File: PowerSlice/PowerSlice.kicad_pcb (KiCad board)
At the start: 2 copper layers, 9 parts, among them U1 PTH08080WAD, U2 PTH08080WAD, U3 INA214BIDCKR, U4 INA214BIDCKR, U5 INA214BIDCKR, U6 NUCLEO-F303K8

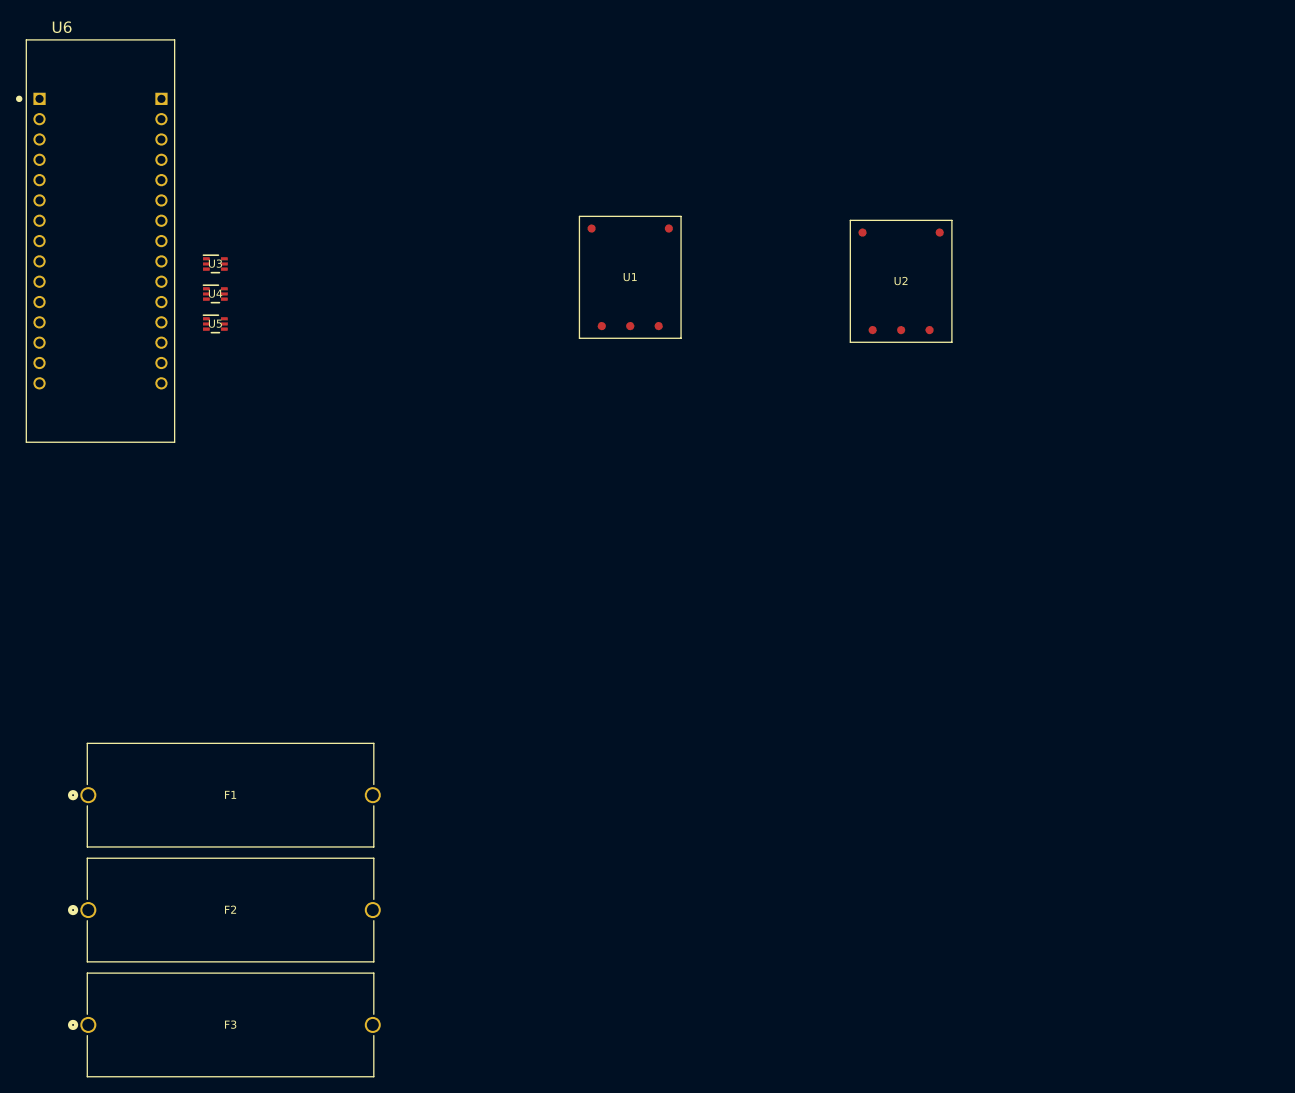
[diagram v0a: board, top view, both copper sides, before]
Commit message: Updated schematic + built PCB
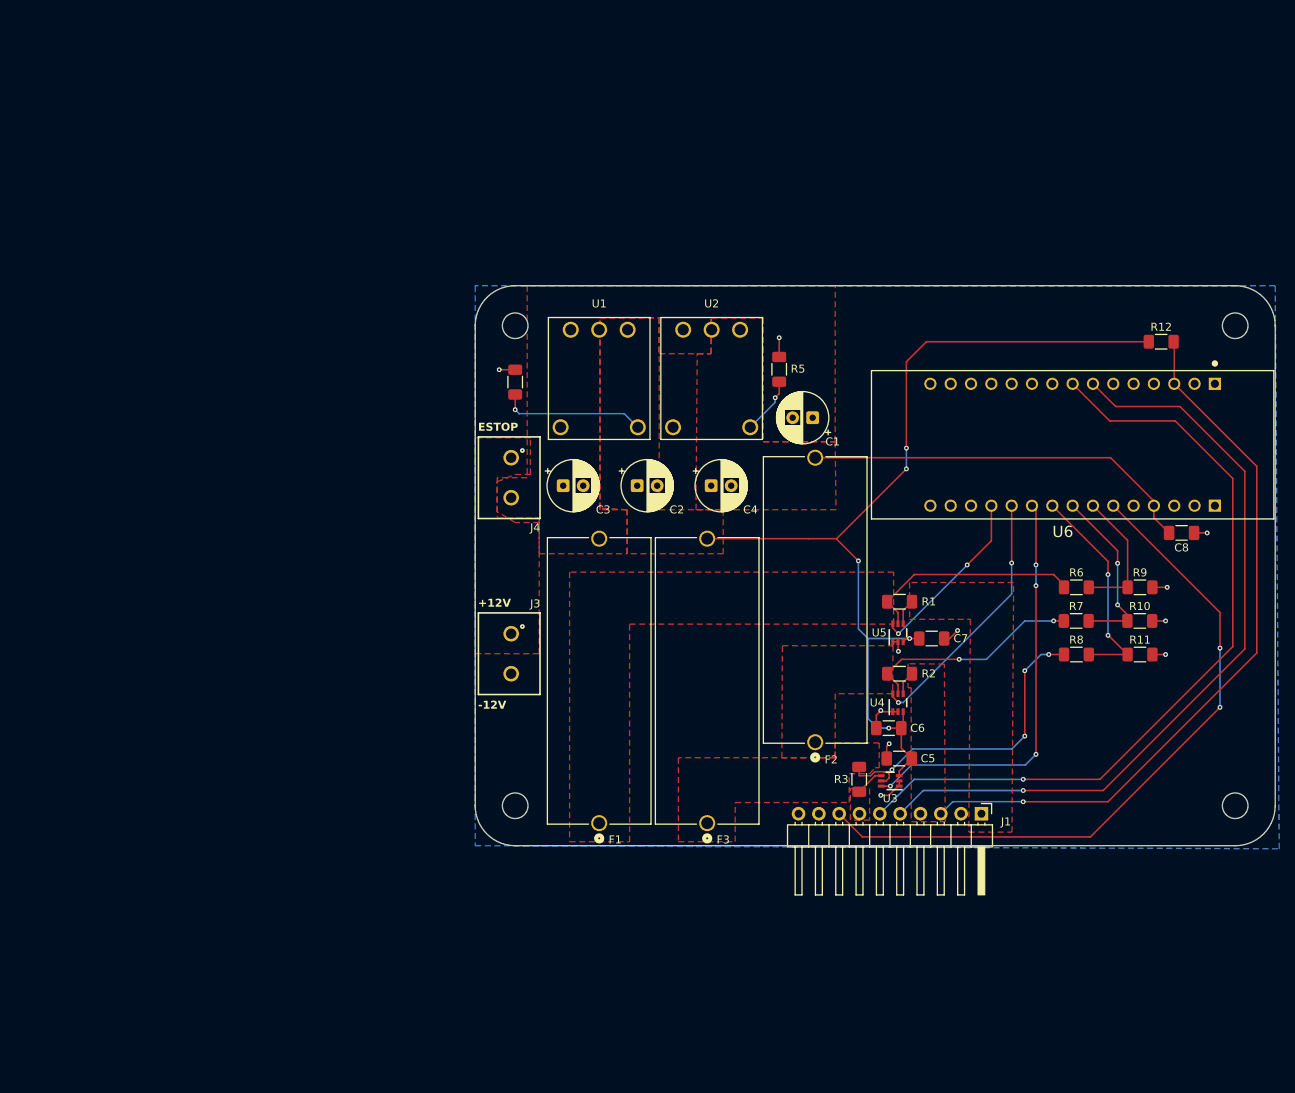
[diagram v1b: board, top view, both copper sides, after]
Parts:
- added C1: 100uF, Capacitor_THT:CP_Radial_D6.3mm_P2.50mm, F.Cu at (116.6, 79.0)
- added C2: 100uF, Capacitor_THT:CP_Radial_D6.3mm_P2.50mm, F.Cu at (94.7, 87.5)
- added C3: 100uF, Capacitor_THT:CP_Radial_D6.3mm_P2.50mm, F.Cu at (85.4, 87.5)
- added C4: 100uF, Capacitor_THT:CP_Radial_D6.3mm_P2.50mm, F.Cu at (103.9, 87.5)
- added C5: 0.1uF, Capacitor_SMD:C_1206_3216Metric_Pad1.33x1.80mm_HandSolder, F.Cu at (127.4, 121.6)
- added C6: 0.1uF, Capacitor_SMD:C_1206_3216Metric_Pad1.33x1.80mm_HandSolder, F.Cu at (126.1, 117.8)
- added C7: 0.1uF, Capacitor_SMD:C_1206_3216Metric_Pad1.33x1.80mm_HandSolder, F.Cu at (131.5, 106.6)
- added C8: 0.1uF, Capacitor_SMD:C_1206_3216Metric_Pad1.33x1.80mm_HandSolder, F.Cu at (162.7, 93.4)
- added J1: Conn_01x10_Pin, Connector_PinHeader_2.54mm:PinHeader_1x10_P2.54mm_Horizontal, F.Cu at (137.7, 128.5)
- added J3: DC_In_Screw, 691137710002:691137710002, F.Cu at (78.9, 108.5)
- added J4: ESTOP, 691137710002:691137710002, F.Cu at (78.9, 86.5)
- added R1: 0.01, Resistor_SMD:R_1206_3216Metric_Pad1.30x1.75mm_HandSolder, F.Cu at (127.5, 102.0)
- added R10: 100k, Resistor_SMD:R_1206_3216Metric_Pad1.30x1.75mm_HandSolder, F.Cu at (157.5, 104.4)
- added R11: 100k, Resistor_SMD:R_1206_3216Metric_Pad1.30x1.75mm_HandSolder, F.Cu at (157.5, 108.6)
- added R12: 100k, Resistor_SMD:R_1206_3216Metric_Pad1.30x1.75mm_HandSolder, F.Cu at (160.2, 69.5)
- added R2: 0.01, Resistor_SMD:R_1206_3216Metric_Pad1.30x1.75mm_HandSolder, F.Cu at (127.5, 111.0)
- added R3: 0.01, Resistor_SMD:R_1206_3216Metric_Pad1.30x1.75mm_HandSolder, F.Cu at (122.4, 124.2)
- added R4: 1.87k, Resistor_SMD:R_1206_3216Metric_Pad1.30x1.75mm_HandSolder, F.Cu at (79.4, 74.5)
- added R5: 348, Resistor_SMD:R_1206_3216Metric_Pad1.30x1.75mm_HandSolder, F.Cu at (112.4, 73.0)
- added R6: 330k, Resistor_SMD:R_1206_3216Metric_Pad1.30x1.75mm_HandSolder, F.Cu at (149.6, 100.2)
- added R7: 330k, Resistor_SMD:R_1206_3216Metric_Pad1.30x1.75mm_HandSolder, F.Cu at (149.5, 104.4)
- added R8: 330k, Resistor_SMD:R_1206_3216Metric_Pad1.30x1.75mm_HandSolder, F.Cu at (149.6, 108.6)
- added R9: 100k, Resistor_SMD:R_1206_3216Metric_Pad1.30x1.75mm_HandSolder, F.Cu at (157.5, 100.2)
- added REF**: MountingHole_3.2mm_M3, MountingHole:MountingHole_3.2mm_M3, F.Cu at (169.4, 67.5)
- added REF**: MountingHole_3.2mm_M3, MountingHole:MountingHole_3.2mm_M3, F.Cu at (169.4, 127.5)
- added REF**: MountingHole_3.2mm_M3, MountingHole:MountingHole_3.2mm_M3, F.Cu at (79.4, 127.5)
- added REF**: MountingHole_3.2mm_M3, MountingHole:MountingHole_3.2mm_M3, F.Cu at (79.4, 67.5)
- moved U6 124.2 mm to (149.1, 82.4), turned to -90 degrees
- moved U3 106.3 mm to (126.3, 124.4), turned to 180 degrees
- moved U4 99.5 mm to (127.3, 114.6), turned to 90 degrees
- moved U5 93.6 mm to (127.3, 105.9), turned to 90 degrees
- moved F2 93.3 mm to (116.9, 119.6), turned to 90 degrees
- moved F3 81.4 mm to (103.4, 129.7), turned to 90 degrees
- moved F1 64.0 mm to (89.9, 129.7), turned to 90 degrees
- moved U2 26.6 mm to (104.0, 74.1), turned to 180 degrees
- moved U1 13.2 mm to (89.9, 74.1), turned to 180 degrees
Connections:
- F1 pad 1: 12V_L -> R1-
- F1 pad 2: R1- -> +12V
- F2 pad 1: 5V_L -> R2-
- F2 pad 2: R2- -> +5V
- F3 pad 1: 3V3_L -> R3-
- F3 pad 2: R3- -> +3V3
- U1 pad 1: R1+ -> +12V
- U1 pad 3: R3+ -> +3V3
- U2 pad 1: R1+ -> +12V
- U2 pad 3: R2+ -> +5V
- U3 pad 3: R3+ -> +3V3
- U4 pad 3: R3+ -> +3V3
- U5 pad 3: R3+ -> +3V3
- U6 pad 3_3: unconnected-(U6A-NRST_1-Pad3_3) -> RESET
- U6 pad 3_4: unconnected-(U6A-GND_1-Pad3_4) -> GND
- U6 pad 3_7: unconnected-(U6A-PB7-Pad3_7) -> SDA
- U6 pad 3_8: unconnected-(U6A-PB6-Pad3_8) -> SCL
- U6 pad 4_10: unconnected-(U6B-PA3-Pad4_10) -> R3_Current
- U6 pad 4_11: unconnected-(U6B-PA1-Pad4_11) -> R2_Current
- U6 pad 4_12: unconnected-(U6B-PA0-Pad4_12) -> R1_Current
- U6 pad 4_2: unconnected-(U6B-GND_2-Pad4_2) -> GND
- U6 pad 4_4: unconnected-(U6B-+5V-Pad4_4) -> +5V
- U6 pad 4_6: unconnected-(U6B-PA7-Pad4_6) -> LED
- U6 pad 4_7: unconnected-(U6B-PA6-Pad4_7) -> 12VSns
- U6 pad 4_8: unconnected-(U6B-PA5-Pad4_8) -> 5VSns
- U6 pad 4_9: unconnected-(U6B-PA4-Pad4_9) -> 3V3Sns
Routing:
- net +3V3: track 0.00 -> 118.7 mm, vias 0 -> 5
- net SCL: track 0.00 -> 98.7 mm, vias 0 -> 1
- net SDA: track 0.00 -> 97.3 mm, vias 0 -> 1
- net RESET: track 0.00 -> 91.1 mm, vias 0 -> 1
- net LED: track 0.00 -> 86.7 mm, vias 0 -> 2
- net R3_Current: track 0.00 -> 52.4 mm, vias 0 -> 4
- net +5V: track 0.00 -> 49.6 mm
- net R3-: track 0.00 -> 40.2 mm, vias 0 -> 4
- net R2_Current: track 0.00 -> 32.2 mm, vias 0 -> 2
- net R2-: track 0.00 -> 27.9 mm, vias 0 -> 2
- net R1-: track 0.00 -> 27.7 mm
- net 3V3Sns: track 0.00 -> 27.4 mm, vias 0 -> 2
- net GND: track 0.00 -> 25.2 mm, vias 0 -> 11
- net R1_Current: track 0.00 -> 22.4 mm, vias 0 -> 2
- net 5VSns: track 0.00 -> 22.1 mm, vias 0 -> 2
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- added copper zone on F.Cu, net +12V
- added copper zone on F.Cu, net +3V3
- added copper zone on F.Cu, net +5V
- added copper zone on B.Cu, net GND
- added copper zone on F.Cu, net Net-(J3-Pin_1)
- added copper zone on F.Cu, net R1+
- added copper zone on F.Cu, net R1-
- added copper zone on F.Cu, net R2+
- added copper zone on F.Cu, net R2-
- added copper zone on F.Cu, net R3+
- added copper zone on F.Cu, net R3-
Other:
- board outline added: 100 x 70 mm
- board text added: "+12V"
- board text added: "-12V"
- board text added: "ESTOP"

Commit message: updated lightly after PCB review TODO: figure out LED and Header pins
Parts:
- removed R12: 100k, Resistor_SMD:R_1206_3216Metric_Pad1.30x1.75mm_HandSolder
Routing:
- net +3V3: track 118.7 -> 61.6 mm, vias 5 -> 3
- net RESET: track 91.1 -> 85.8 mm
- net R1-: track 27.7 -> 28.6 mm

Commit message: Wacky stuff that needs to be changed cuz it wont work and will be reverted
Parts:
- added J5: +12V_Screw, 691137710002:691137710002, F.Cu at (167.3, 96.3)
- added J6: +5V_Screw, 691137710002:691137710002, F.Cu at (167.3, 107.4)
- added J7: +3V3_Screw, 691137710002:691137710002, F.Cu at (167.3, 118.6)
- moved C8 3.50 mm to (159.2, 93.4), turned to 90 degrees
- moved U6 1.50 mm to (149.1, 80.9)
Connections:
- J1 pad 1: R1+ -> +12V_L
- J1 pad 2: unconnected-(J1-Pin_2-Pad2) -> RESET
- J1 pad 3: RESET -> +3V3_L
- J1 pad 4: R2+ -> SDA
- J1 pad 5: SDA -> SCL
- J1 pad 6: SCL -> +5V_L
- J1 pad 7: R3+ -> LED
- J1 pad 8: LED -> GND
- J1 pad 9: unconnected-(J1-Pin_9-Pad9) -> E_STOP
- R1 pad 1: R1+ -> +12V_L
- R2 pad 1: R2+ -> +5V_L
- R3 pad 1: R3+ -> +3V3_L
- U6 pad 3_14: unconnected-(U6A-PB5-Pad3_14) -> E_STOP
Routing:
- net SCL: track 98.7 -> 0.00 mm, vias 1 -> 0
- net SDA: track 97.3 -> 0.00 mm, vias 1 -> 0
- net LED: track 86.7 -> 0.00 mm, vias 2 -> 0
- net RESET: track 85.8 -> 0.00 mm, vias 1 -> 0
- net 3V3Sns: track 27.4 -> 17.5 mm
- net 5VSns: track 22.1 -> 14.1 mm
- net R1_Current: track 22.4 -> 15.1 mm
- net R3_Current: track 52.3 -> 45.6 mm
- net R2_Current: track 32.2 -> 25.7 mm
- net 12VSns: track 16.8 -> 10.7 mm
- net +5V: track 49.6 -> 47.6 mm
- net GND: track 25.2 -> 26.2 mm
- added copper zone on F.Cu, net +12V_L
- added copper zone on F.Cu, net +3V3_L
- added copper zone on F.Cu, net +5V_L
- removed copper zone on F.Cu, net R1+
- removed copper zone on F.Cu, net R2+
- removed copper zone on F.Cu, net R3+
- removed copper zone on F.Cu, net R3-

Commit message: Work, TODO: figure out external power connectors
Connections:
- J1 pad 3: +3V3_L -> +5V_L
- J1 pad 6: +5V_L -> +3V3_L
- U3 pad 4: R3+ -> +3V3_L
- U4 pad 4: R2+ -> +5V_L
- U5 pad 4: R1+ -> +12V_L
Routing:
- net E_STOP: track 0.00 -> 146.1 mm, vias 0 -> 2
- net SCL: track 0.00 -> 122.2 mm
- net SDA: track 0.00 -> 113.9 mm
- net LED: track 0.00 -> 109.3 mm, vias 0 -> 3
- net RESET: track 0.00 -> 91.0 mm
- net 3V3Sns: track 17.5 -> 28.9 mm
- net 5VSns: track 14.1 -> 23.6 mm
- net R1_Current: track 15.1 -> 23.9 mm
- net R3_Current: track 45.6 -> 53.8 mm
- net R2_Current: track 25.7 -> 33.7 mm
- net 12VSns: track 10.7 -> 18.3 mm
- net R3+: track 3.58 -> 0.00 mm
- net +3V3_L: track 0.00 -> 3.58 mm
- net R1+: track 3.21 -> 0.00 mm
- net +12V_L: track 0.00 -> 3.21 mm
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- added copper zone on F.Cu, net R3-

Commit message: "Final" edits before submission for ordering
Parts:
- removed J5: +12V_Screw, 691137710002:691137710002
- removed J6: +5V_Screw, 691137710002:691137710002
- removed J7: +3V3_Screw, 691137710002:691137710002
- added TP1: TestPoint, TestPoint:TestPoint_Keystone_5005-5009_Compact, F.Cu at (123.0, 67.0)
- added TP10: TestPoint, TestPoint:TestPoint_Keystone_5005-5009_Compact, F.Cu at (165.9, 102.7)
- added TP11: TestPoint, TestPoint:TestPoint_Keystone_5005-5009_Compact, F.Cu at (165.9, 109.4)
- added TP12: TestPoint, TestPoint:TestPoint_Keystone_5005-5009_Compact, F.Cu at (165.9, 116.1)
- added TP13: TestPoint, TestPoint:TestPoint_Keystone_5005-5009_Compact, F.Cu at (153.7, 67.0)
- added TP14: TestPoint, TestPoint:TestPoint_Keystone_5005-5009_Compact, F.Cu at (147.2, 67.0)
- added TP2: TestPoint, TestPoint:TestPoint_Keystone_5005-5009_Compact, F.Cu at (128.7, 67.0)
- added TP3: TestPoint, TestPoint:TestPoint_Keystone_5005-5009_Compact, F.Cu at (134.4, 67.0)
- added TP4: TestPoint, TestPoint:TestPoint_Keystone_5005-5009_Compact, F.Cu at (140.1, 67.0)
- added TP5: TestPoint, TestPoint:TestPoint_Keystone_5005-5009_Compact, F.Cu at (139.8, 94.5)
- added TP6: TestPoint, TestPoint:TestPoint_Keystone_5005-5009_Compact, F.Cu at (135.2, 94.5)
- added TP7: TestPoint, TestPoint:TestPoint_Keystone_5005-5009_Compact, F.Cu at (130.6, 94.5)
- added TP8: TestPoint, TestPoint:TestPoint_Keystone_5005-5009_Compact, F.Cu at (125.9, 94.5)
- added TP9: TestPoint, TestPoint:TestPoint_Keystone_5005-5009_Compact, F.Cu at (165.9, 96.1)
- renumbered C3 to C1, C4 to C2, C1 to C3, C2 to C4, C7 to C5, C5 to C7, U5 to U3, U3 to U5
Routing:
- net +3V3: track 61.6 -> 94.9 mm, vias 3 -> 6
- net +5V: track 47.6 -> 69.4 mm
- net R3_Current: track 53.8 -> 69.1 mm
- net +12V: track 0.00 -> 14.6 mm
- net 3V3Sns: track 28.9 -> 40.3 mm
- net 12VSns: track 18.3 -> 29.7 mm
- net 5VSns: track 23.6 -> 34.3 mm
- net R2_Current: track 33.7 -> 42.9 mm, vias 2 -> 3
- net SCL: track 122.2 -> 127.7 mm
- net SDA: track 113.9 -> 118.9 mm
- net R1_Current: track 23.9 -> 27.7 mm
- net RESET: track 91.0 -> 88.3 mm
- net LED: track 109.3 -> 108.2 mm
- net R1-: track 28.6 -> 27.7 mm
- net GND: track 24.6 -> 24.0 mm
